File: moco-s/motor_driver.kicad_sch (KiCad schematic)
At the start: 72 parts, among them Q3 CSD18540Q5B, Q4 CSD18540Q5B, Q5 CSD18540Q5B, Q6 CSD18540Q5B, Q7 CSD18540Q5B, Q8 CSD18540Q5B, U2 DRV8301

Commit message: Comp MoCo-S
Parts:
- removed C4: 22uF/50V, Capacitor_SMD:C_1210_3225Metric_Pad1.33x2.70mm_HandSolder, symbol Device:C
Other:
- moved on the sheet: C14, C20, C31, C32, C33, C34, C35, C36, C5, C7, R46, TH1

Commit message: Update ref
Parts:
- renumbered C15 to C10, C16 to C11, C17 to C12, C18 to C13, C19 to C14, C20 to C15, C21 to C16, C22 to C17, C23 to C18, C24 to C19, C25 to C20, C26 to C21, C27 to C22, C28 to C23, C29 to C24, C30 to C25, C36 to C26, C31 to C27, C5 to C28, C7 to C29, C32 to C30, C33 to C31, C35 to C32, C34 to C33, C1 to C34, C3 to C35, C9 to C4, C10 to C5, C11 to C6, C12 to C7, C13 to C8, C14 to C9, Q3 to Q1, Q4 to Q2, Q5 to Q3, Q6 to Q4, Q7 to Q5, Q8 to Q6, R24 to R13, R25 to R14, R26 to R15, R27 to R16, R28 to R17, R29 to R18, R30 to R19, R31 to R20, R32 to R21, R33 to R22, R34 to R23, R35 to R24, R36 to R25, R37 to R26, R38 to R27, R39 to R28, R40 to R29, R41 to R30, R42 to R31, R43 to R32, R44 to R33, R45 to R34, R46 to R35, TP4 to TP3

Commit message: Use kelvin connection for shunt resistance
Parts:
- C8: JLCPCB Part # (none) -> C114405; MFR.Part # (none) -> CC0402KRX7R9BB153
- J?: MFR.Part # (none) -> MR30PB-F
- R22: JLCPCB Part # (none) -> C25767; MFR.Part # (none) -> 0402WGF2203TCE
- R27, R32: JLCPCB Part # (none) -> C469426; MFR.Part # (none) -> ASR-M-3-0.5F
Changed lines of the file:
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@@
     )
     (property "Note" "${REFERENCE} connect to motor" (id 4) (at 237.49 41.91 0))
+    (property "MFR.Part #" "MR30PB-F" (id 5) (at 209.55 43.18 0)
+      (effects (font (size 1.27 1.27)) hide)
+    )
     (pin "1")
     (pin "2")
@@
     )
     (property "Datasheet" "~" (id 3) (at 71.12 120.65 0)
+      (effects (font (size 1.27 1.27)) hide)
+    )
+    (property "JLCPCB Part #" "C25767" (id 4) (at 71.12 120.65 0)
+      (effects (font (size 1.27 1.27)) hide)
+    )
+    (property "MFR.Part #" "0402WGF2203TCE" (id 5) (at 71.12 120.65 0)
       (effects (font (size 1.27 1.27)) hide)
     )
@@
       (effects (font (size 1.27 1.27)) hide)
     )
+    (property "JLCPCB Part #" "C469426" (id 4) (at 161.29 62.23 0)
+      (effects (font (size 1.27 1.27)) hide)
+    )
+    (property "MFR.Part #" "ASR-M-3-0.5F" (id 5) (at 161.29 62.23 0)
+      (effects (font (size 1.27 1.27)) hide)
+    )
     (pin "1")
     (pin "2")
@@
       (effects (font (size 1.27 1.27)) hide)
     )
+    (property "JLCPCB Part #" "C114405" (id 4) (at 60.96 118.11 0)
+      (effects (font (size 1.27 1.27)) hide)
+    )
+    (property "MFR.Part #" "CC0402KRX7R9BB153" (id 5) (at 60.96 118.11 0)
+      (effects (font (size 1.27 1.27)) hide)
+    )
     (pin "1")
     (pin "2")
@@
       (effects (font (size 1.27 1.27)) hide)
     )
+    (property "JLCPCB Part #" "C469426" (id 4) (at 104.14 60.96 0)
+      (effects (font (size 1.27 1.27)) hide)
+    )
+    (property "MFR.Part #" "ASR-M-3-0.5F" (id 5) (at 104.14 60.96 0)
+      (effects (font (size 1.27 1.27)) hide)
+    )

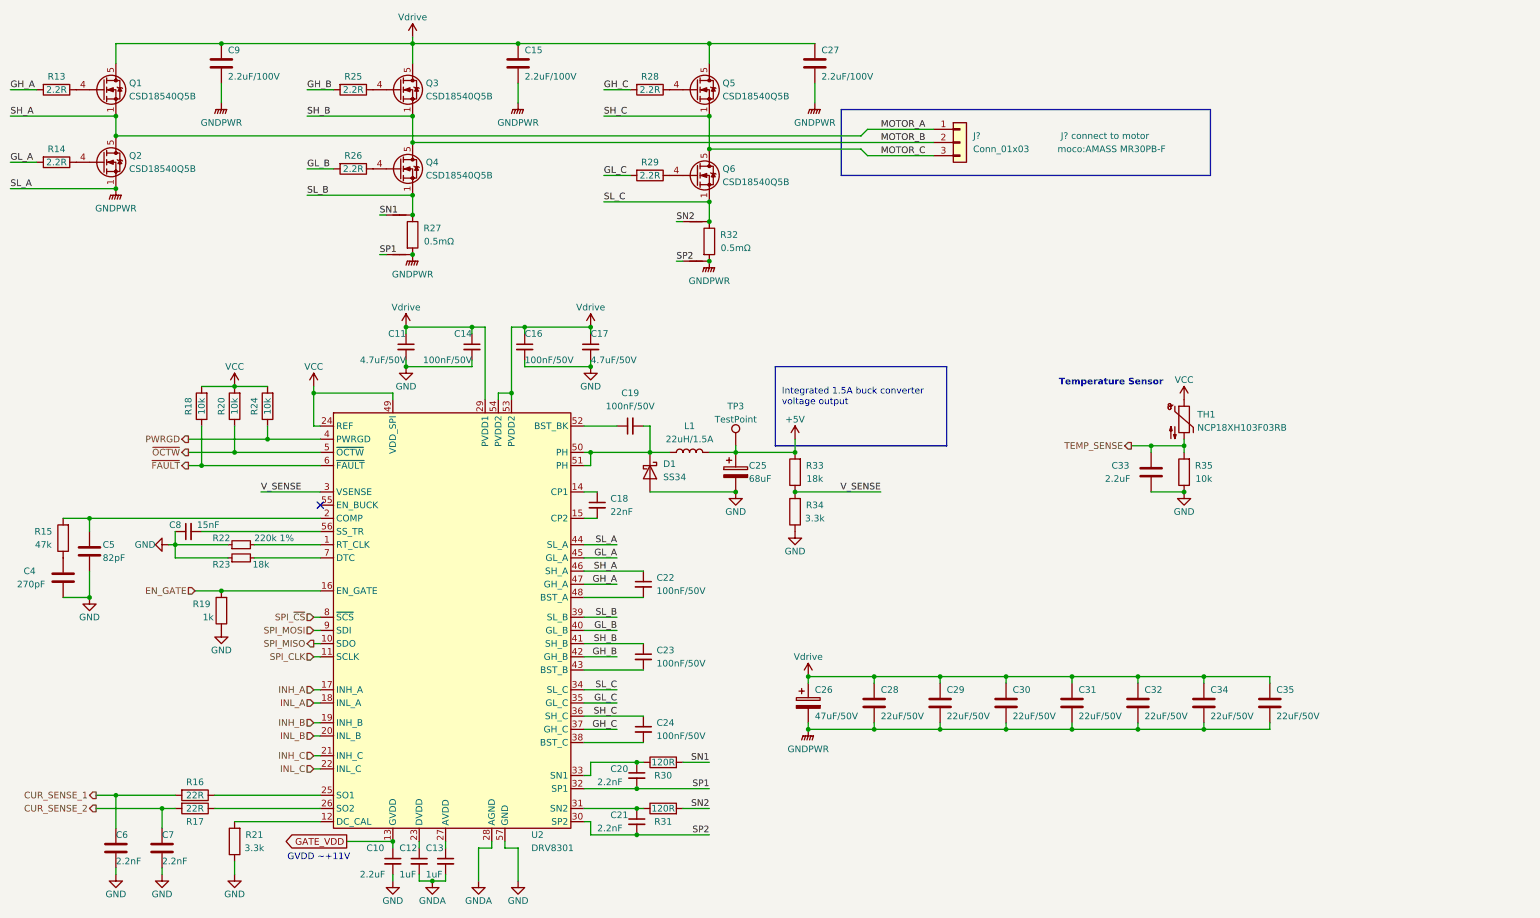
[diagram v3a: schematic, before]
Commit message: Replace some extended parts to basic parts
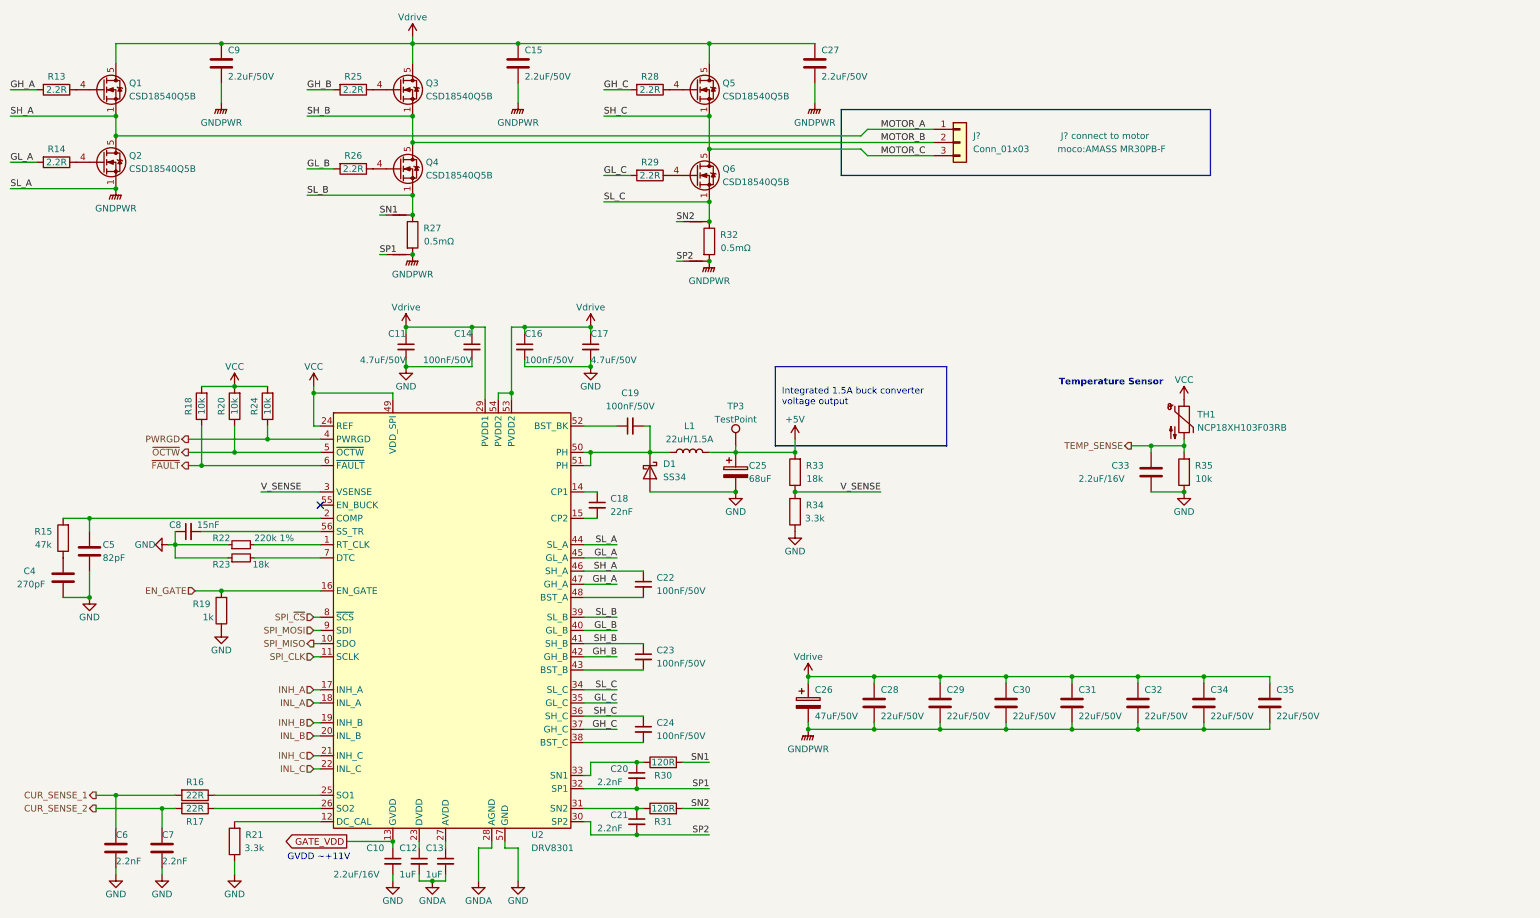
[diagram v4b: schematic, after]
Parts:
- C10, C33: value 2.2uF -> 2.2uF/16V; Basic Part (none) -> N
- C11, C12, C13, C14, C16, C17, C18, C19, C20, C21, C22, C23, C24, C28, C29, C30, C31, C32, C34, C35, C6, C7, D1, R15, R16, R17, R18, R19, R20, R21, R22, R23, R24, R30, R31, R33, R34, R35: Basic Part (none) -> Y
- C15, C27, C9: value 2.2uF/100V -> 2.2uF/50V; Basic Part (none) -> Y; JLCPCB Part # C650969 -> C50254; MFR.Part # HMK316AC7225KLHTE -> CL31B225KBHNNNE
- C25, C26, C4, C5, C8, J?, L1, Q1, Q2, Q3, Q4, Q5, Q6, R27, R32, TH1, U2: Basic Part (none) -> N
- R13, R14, R25, R26, R28, R29: Basic Part (none) -> Y; JLCPCB Part # C25226 -> C22939; MFR.Part # 0603WAJ022JT5E -> 0603WAF220KT5E
